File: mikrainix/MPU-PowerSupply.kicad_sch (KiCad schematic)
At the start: 85 parts, among them Q5 2N7002, U7 RV1106G3, U8 TPS65262-1RHBT

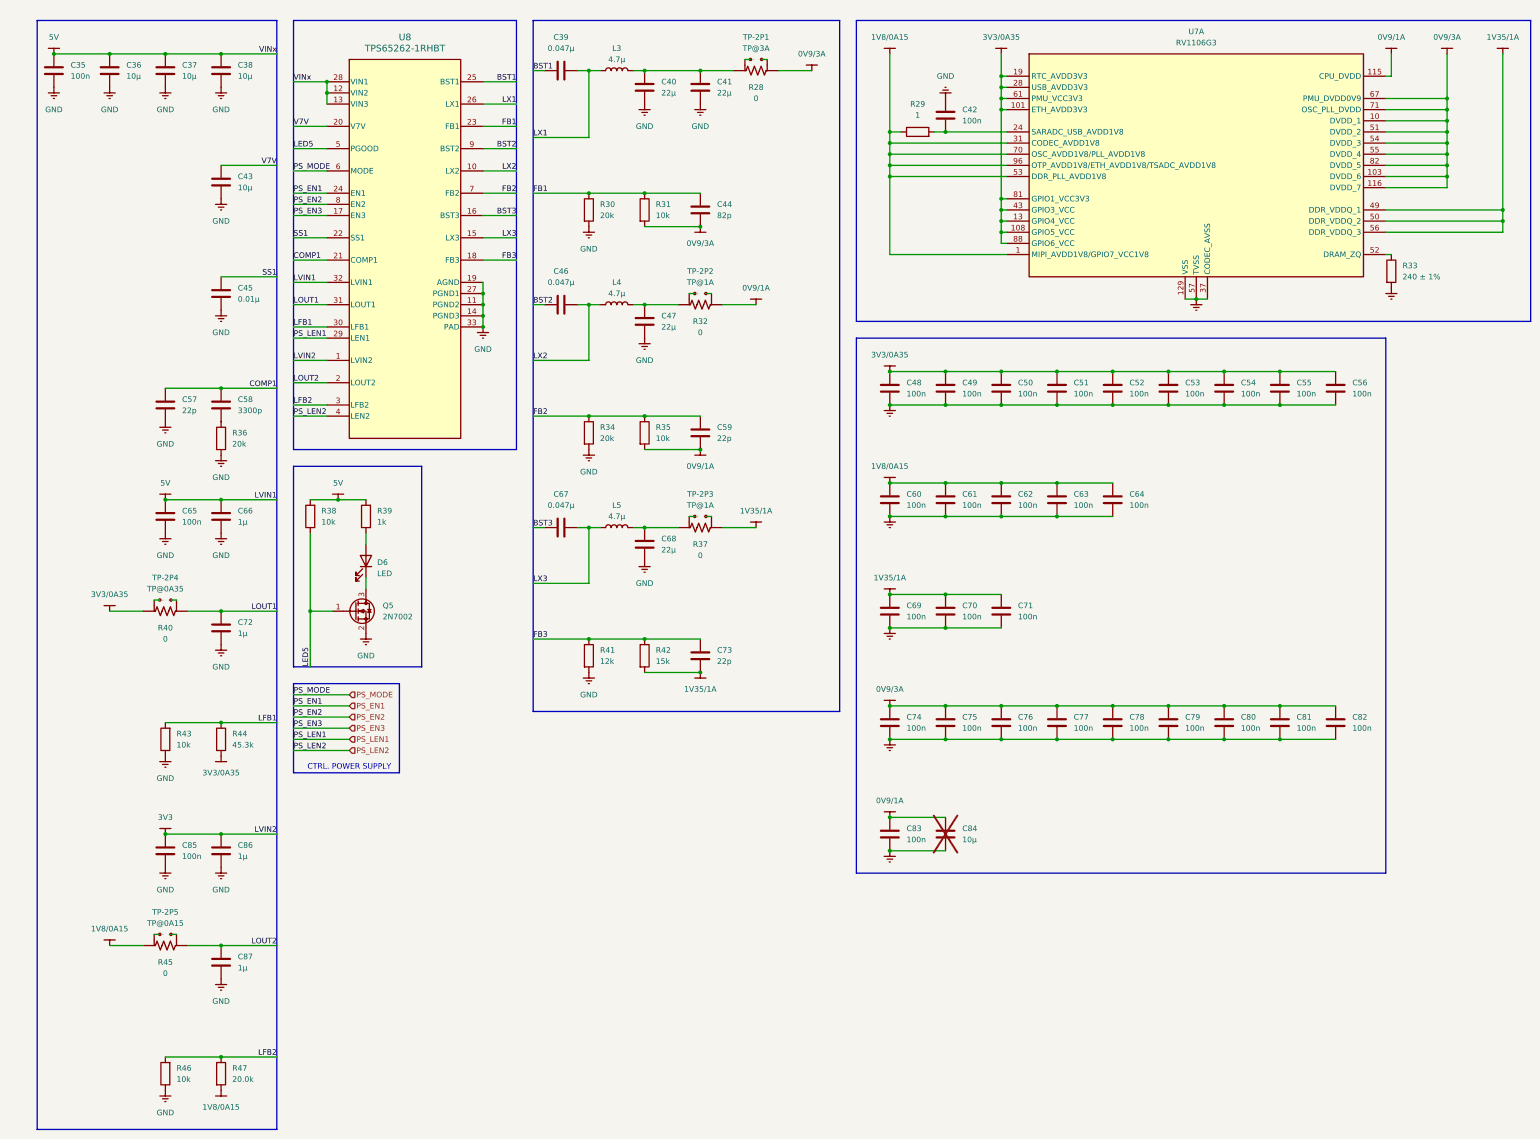
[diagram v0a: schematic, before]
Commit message: add MIS5001 camera and Ethernet, replace ESP32-C6-MINI > ESP32-MINI-1
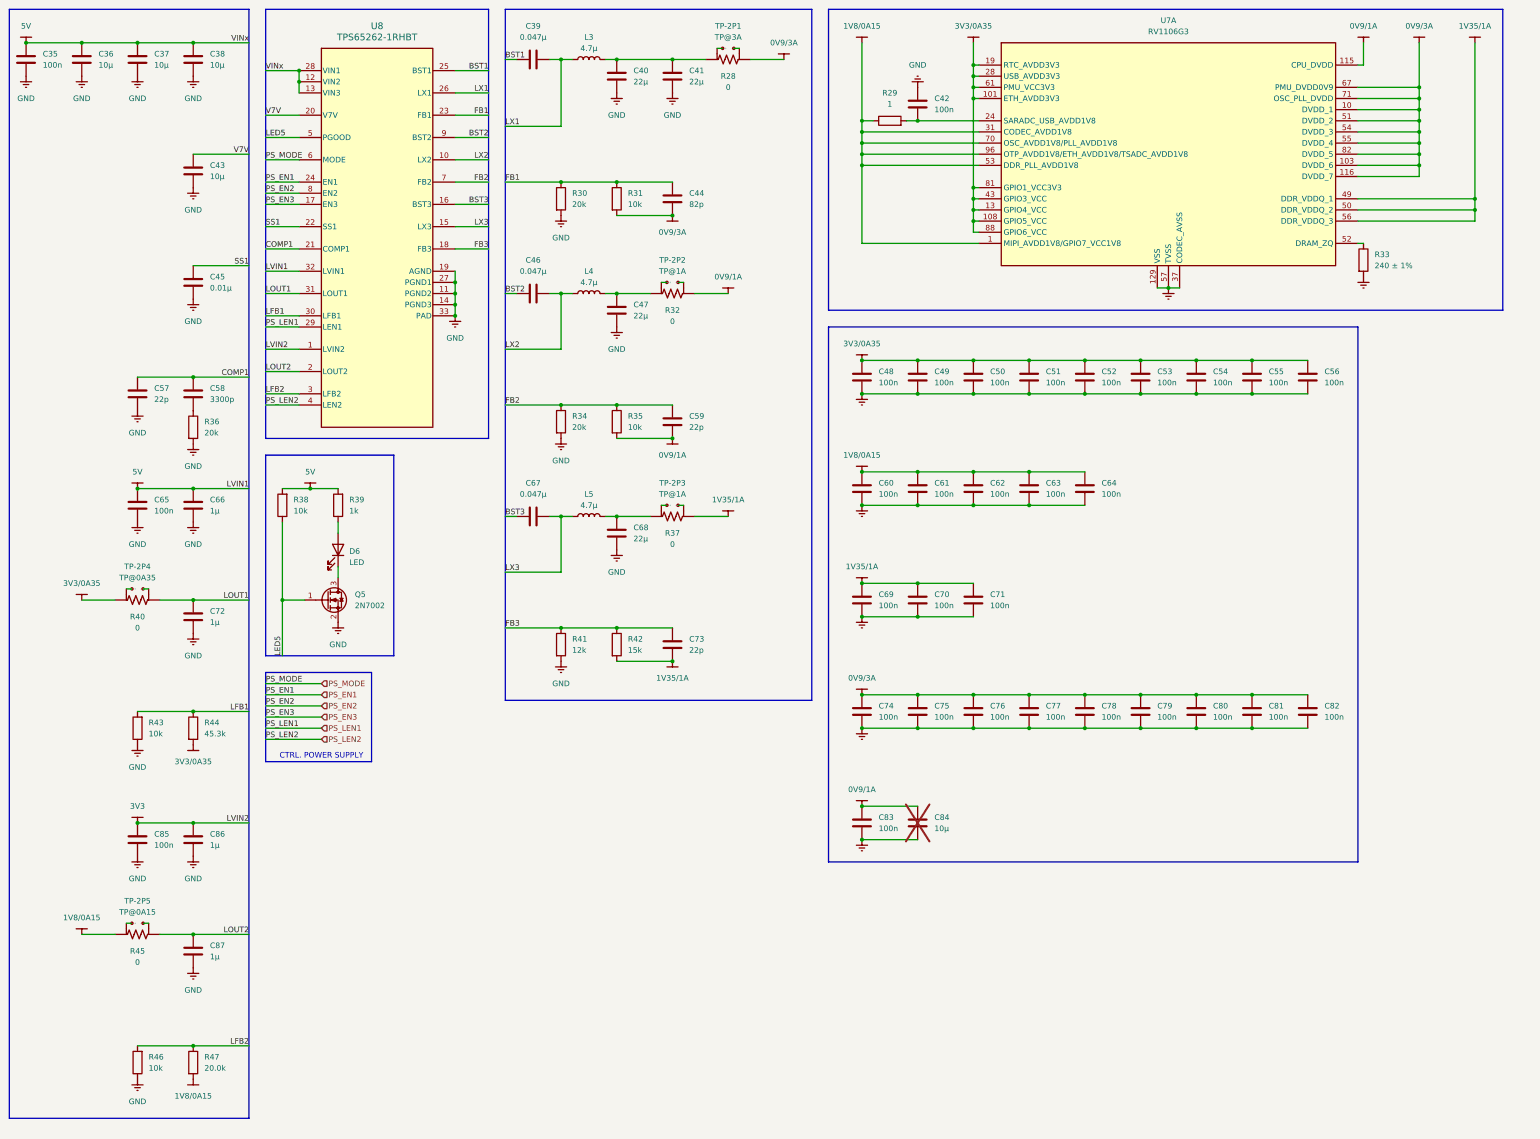
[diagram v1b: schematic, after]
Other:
- moved on the sheet: C35, C36, C37, C38, C39, C40, C41, C42, C43, C44, C45, C46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

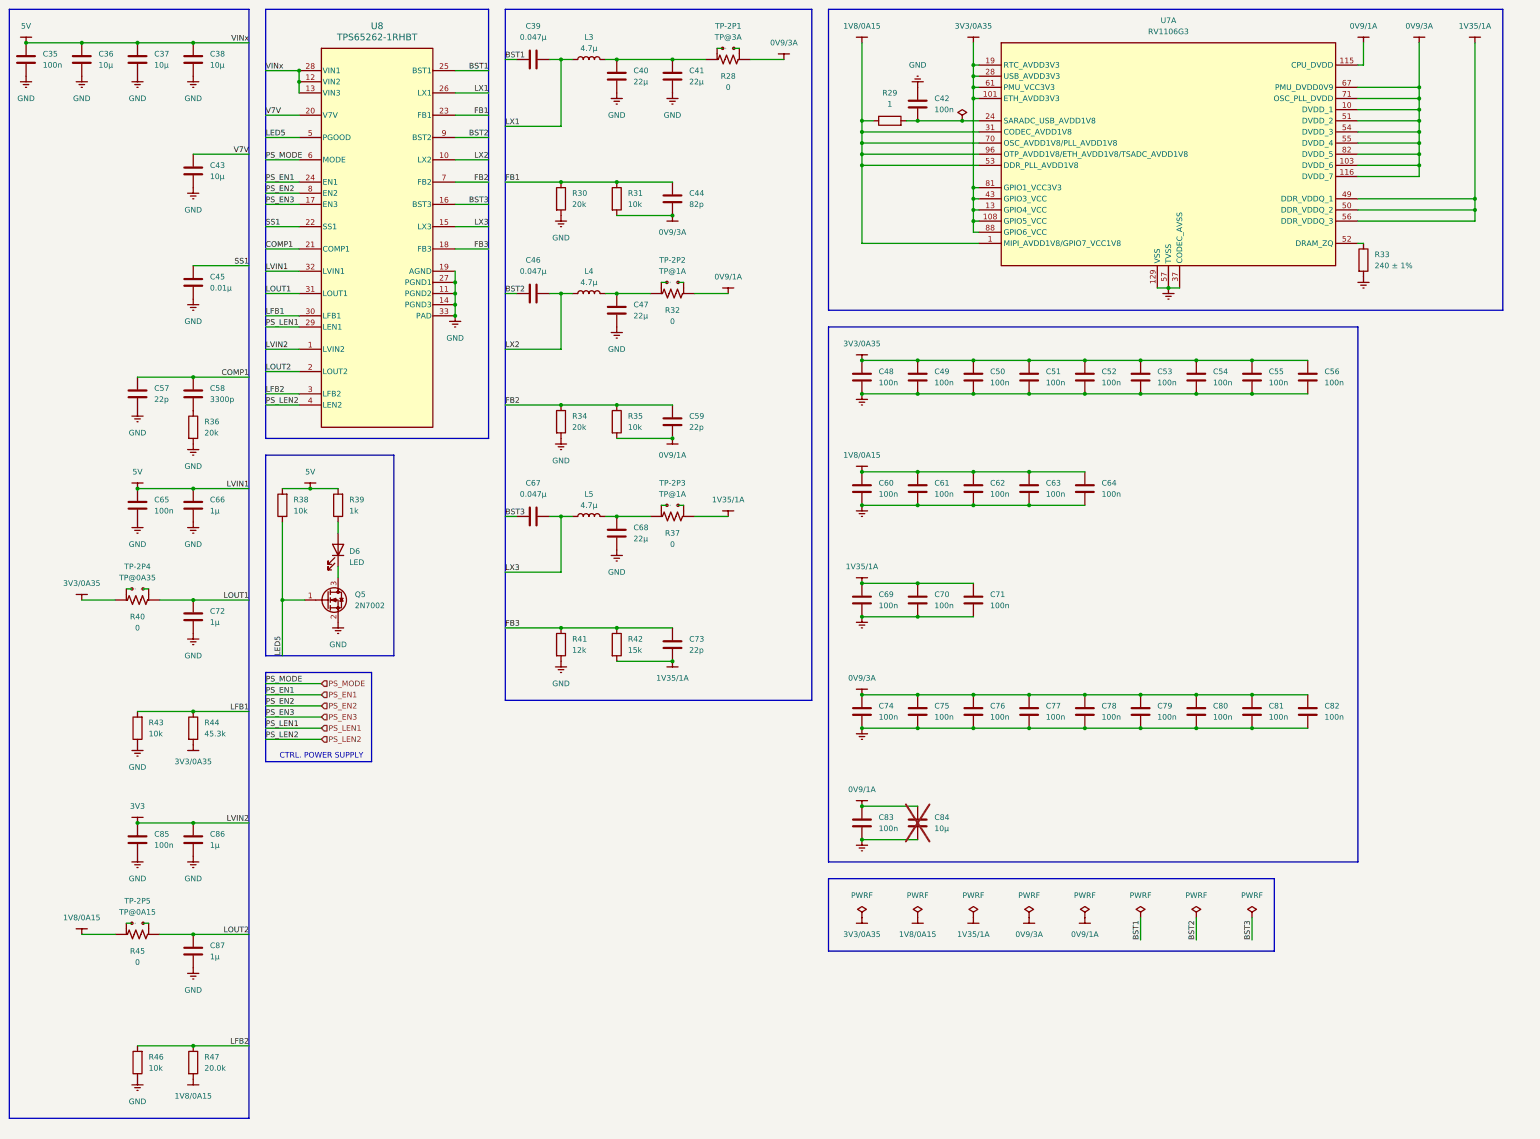
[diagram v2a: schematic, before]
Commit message: add ESD protection
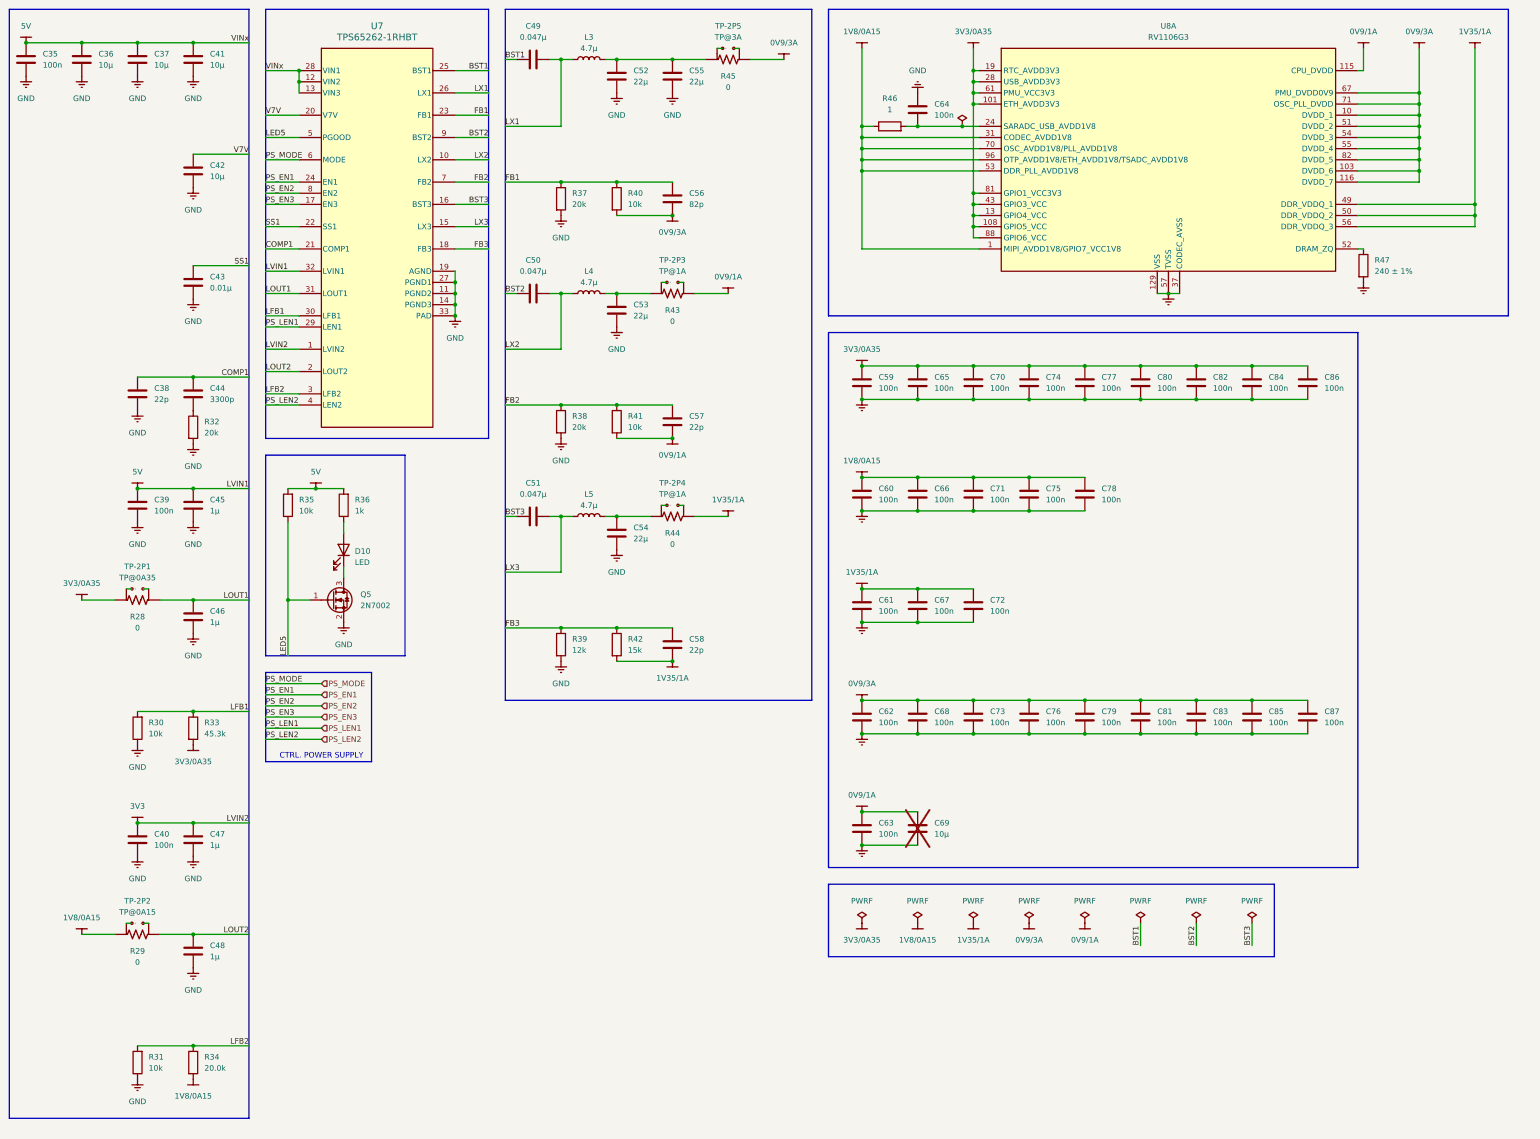
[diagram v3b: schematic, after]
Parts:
- removed R28, R32, R37, R40, R45: 0, mikrainix-2345986-1:TE_2345986-1, symbol mikrainix-R_SHUNT:R_SHUNT
- removed U7: RV1106G3, mikrainix-RV1106G3:QFN35P1230X1230X90-129N, symbol mikrainix-RV1106G3:RV1106G3
- removed U8: TPS65262-1RHBT, mikrainix-TPS65262-1RHBT:RHB0032E_NV, symbol mikrainix-TPS65262-1RHBT:TPS65262-1RHBT
- added R28, R29, R43, R44, R45: 0, symbol mikrainix-R_SHUNT_SYM:R_SHUNT
- added U7: TPS65262-1RHBT, mikrainix-TPS65262-1RHBT:RHB0032E_NV, symbol mikrainix-TPS65262-1RHBT:TPS65262-1RHBT
- added U8: RV1106G3, mikrainix-RV1106G3:QFN35P1230X1230X90-129N, symbol mikrainix-RV1106G3:RV1106G3
- TP-2P1: value TP@3A -> TP@0A35
- TP-2P2: value TP@1A -> TP@0A15
- TP-2P4: value TP@0A35 -> TP@1A
- TP-2P5: value TP@0A15 -> TP@3A
- renumbered C57 to C38, C65 to C39, C85 to C40, C38 to C41, C43 to C42, C45 to C43, C58 to C44, C66 to C45, C72 to C46, C86 to C47, C87 to C48, C39 to C49, C46 to C50, C67 to C51, C40 to C52, C47 to C53, C68 to C54, C41 to C55, C44 to C56, C59 to C57, C73 to C58, C48 to C59, C69 to C61, C74 to C62, C83 to C63, C42 to C64, C49 to C65, C61 to C66, C70 to C67, C75 to C68, C84 to C69, C50 to C70, C62 to C71, C71 to C72, C76 to C73, C51 to C74, C63 to C75, C77 to C76, C52 to C77, C64 to C78, C78 to C79, C53 to C80, C79 to C81, C54 to C82, C80 to C83, C55 to C84, C81 to C85, C56 to C86, C82 to C87, D6 to D10, R43 to R30, R46 to R31, R36 to R32, R44 to R33, R47 to R34, R38 to R35, R39 to R36, R30 to R37, R34 to R38, R41 to R39, R31 to R40, R35 to R41, R29 to R46, R33 to R47
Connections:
- net 0V9/1A: now also R43.4, U8.115 (CPU_DVDD)
- net 0V9/3A: now also R45.4, U8.10 (DVDD_1), U8.103 (DVDD_6), U8.116 (DVDD_7), U8.51 (DVDD_2), U8.54 (DVDD_3), U8.55 (DVDD_4), U8.67 (PMU_DVDD0V9), U8.71 (OSC_PLL_DVDD), U8.82 (DVDD_5)
- net 1V35/1A: now also R44.4, U8.49 (DDR_VDDQ_1), U8.50 (DDR_VDDQ_2), U8.56 (DDR_VDDQ_3)
- net 1V8/0A15: now also R29.1, U8.1 (MIPI_AVDD1V8/GPIO7_VCC1V8), U8.31 (CODEC_AVDD1V8), U8.53 (DDR_PLL_AVDD1V8), U8.70 (OSC_AVDD1V8/PLL_AVDD1V8), U8.96 (OTP_AVDD1V8/ETH_AVDD1V8/TSADC_AVDD1V8)
- net 3V3: now also U7.1 (LVIN2)
- net 3V3/0A35: now also R28.1, U8.101 (ETH_AVDD3V3), U8.108 (GPIO5_VCC), U8.13 (GPIO4_VCC), U8.19 (RTC_AVDD3V3), U8.28 (USB_AVDD3V3), U8.43 (GPIO3_VCC), U8.61 (PMU_VCC3V3), U8.81 (GPIO1_VCC3V3), U8.88 (GPIO6_VCC)
- net 5V: now also U7.12 (VIN2), U7.13 (VIN3), U7.28 (VIN1), U7.32 (LVIN1)
- net BST1: now also U7.25 (BST1)
- net BST2: now also U7.9 (BST2)
- net BST3: now also U7.16 (BST3)
- net COMP1: now also U7.21 (COMP1)
- net FB1: now also U7.23 (FB1)
- net FB2: now also U7.7 (FB2)
- net FB3: now also U7.18 (FB3)
- net GND: now also U7.11 (PGND2), U7.14 (PGND3), U7.19 (AGND), U7.27 (PGND1), U7.33 (PAD), U8.129 (VSS), U8.37 (CODEC_AVSS), U8.57 (TVSS)
- net LED5: now also U7.5 (PGOOD)
- net LFB1: now also U7.30 (LFB1)
- net LFB2: now also U7.3 (LFB2)
- net LOUT1: now also R28.4, U7.31 (LOUT1)
- net LOUT2: now also R29.4, U7.2 (LOUT2)
- net LX1: now also U7.26 (LX1)
- net LX2: now also U7.10 (LX2)
- net LX3: now also U7.15 (LX3)
- net PS_EN1: now also U7.24 (EN1)
- net PS_EN2: now also U7.8 (EN2)
- net PS_EN3: now also U7.17 (EN3)
- net PS_LEN1: now also U7.29 (LEN1)
- net PS_LEN2: now also U7.4 (LEN2)
- net PS_MODE: now also U7.6 (MODE)
- net SS1: now also U7.22 (SS1)
- net V7V: now also U7.20 (V7V)
- net at C54.1, L5.2: now also R44.1
- net at C52.1, C55.1, L3.2: now also R45.1
- net at TP-2P5.1 (+): now also R45.2
- net at TP-2P5.2 (-): now also R45.3
- net at C53.1, L4.2: now also R43.1
- net at TP-2P2.1 (+): now also R29.2
- net at TP-2P2.2 (-): now also R29.3
- net at TP-2P3.1 (+): now also R43.2
- net at TP-2P3.2 (-): now also R43.3
- net at TP-2P1.1 (+): now also R28.2
- net at TP-2P1.2 (-): now also R28.3
- net at TP-2P4.1 (+): now also R44.2
- net at TP-2P4.2 (-): now also R44.3
- net at C64.2, R46.2: now also U8.24 (SARADC_USB_AVDD1V8)
- net at R47.1: now also U8.52 (DRAM_ZQ)
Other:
- moved on the sheet: C59, C60, C61, C62, C63, C64, C65, C66, C67, C68, C69, C70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
